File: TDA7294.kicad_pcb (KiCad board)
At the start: 2 copper layers, 81 x 58 mm, 42 parts, among them J1 PAWER, J2 OUT, J3 IN, U1 TDA7294, U2 TDA7294

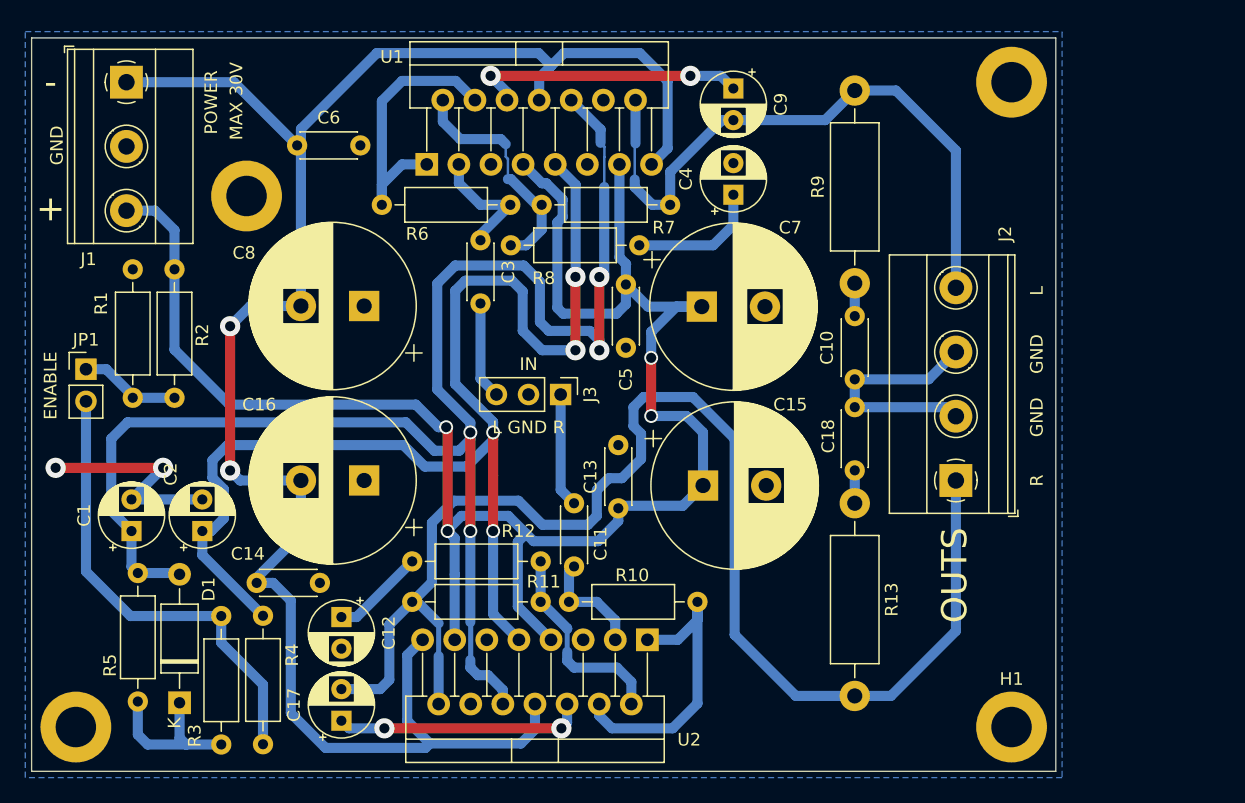
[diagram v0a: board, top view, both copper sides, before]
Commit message: completada version 1.1.0 con TDA al mismo lado
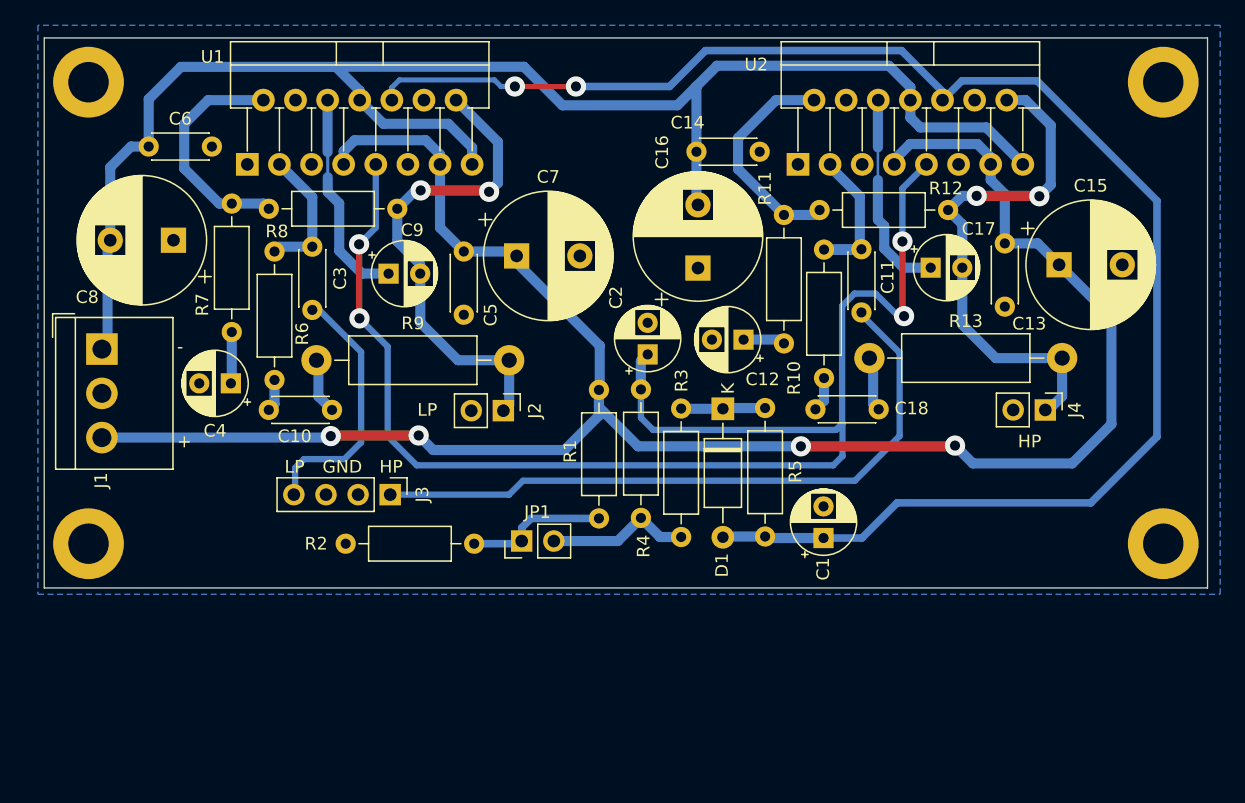
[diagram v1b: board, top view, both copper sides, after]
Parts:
- added J4: Conn_01x02, Connector_PinHeader_2.54mm:PinHeader_1x02_P2.54mm_Vertical, F.Cu at (187.2, 99.4)
- C15, C16, C7, C8: footprint Capacitor_THT:CP_Radial_D13.0mm_P5.00mm -> Capacitor_THT:CP_Radial_D10.0mm_P5.00mm
- J1: footprint TerminalBlock_Phoenix:TerminalBlock_Phoenix_MKDS-1,5-3-5.08_1x03_P5.08mm_Horizontal -> MR-footprint:TerminalBlock_1x03_P3.50mm_Vertical
- J2: value OUT -> Conn_01x02; footprint TerminalBlock_Phoenix:TerminalBlock_Phoenix_MKDS-1,5-4-5.08_1x04_P5.08mm_Horizontal -> Connector_PinHeader_2.54mm:PinHeader_1x02_P2.54mm_Vertical
- J3: footprint Connector_PinHeader_2.54mm:PinHeader_1x03_P2.54mm_Vertical -> Connector_PinHeader_2.54mm:PinHeader_1x04_P2.54mm_Vertical
- moved H2 100.0 mm to (196.5, 73.5)
- moved H3 81.6 mm to (111.5, 110.0)
- moved C17 58.8 mm to (178.1, 88.2), turned to 0 degrees
- moved C1 54.7 mm to (169.6, 109.5)
- moved R12 52.5 mm to (179.5, 83.6), turned to 180 degrees
- moved R5 49.7 mm to (165.0, 109.4), turned to 90 degrees
- moved D1 48.9 mm to (161.7, 99.3), turned to -90 degrees
- moved C14 48.7 mm to (159.6, 79.0)
- moved C10 46.4 mm to (125.8, 99.4), turned to 0 degrees
- moved R3 45.0 mm to (158.4, 99.3), turned to -90 degrees
- moved R9 43.0 mm to (129.5, 95.5), turned to 0 degrees
- moved C4 42.4 mm to (122.8, 97.3), turned to 180 degrees
- moved U2 39.4 mm to (167.6, 80.0), turned to 0 degrees
- moved C12 38.6 mm to (163.3, 93.9), turned to 180 degrees
- moved C2 37.9 mm to (155.7, 95.0)
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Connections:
- J2 pad 1: /OUT2 -> /OUT1
- J3 pad 3: /IN1 -> GND
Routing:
- net GND: track 83.7 -> 5.31 mm, vias 2 -> 0
- net /OUT2: track 111.6 -> 41.3 mm, vias 0 -> 2
- net /IN2: track 9.04 -> 53.2 mm
- net /-VS: track 150.9 -> 124.2 mm, vias 2 -> 0
- net Net-(JP1-B): track 37.1 -> 11.5 mm
- net /+VS: track 146.0 -> 159.4 mm
- net /STBY: track 99.7 -> 112.7 mm
- net /IN1: track 7.72 -> 20.6 mm
- net /OUT1: track 51.0 -> 39.0 mm, vias 0 -> 2
- net Net-(C4-Pad1): track 10.5 -> 4.09 mm
- net Net-(D1-K): track 13.1 -> 6.67 mm
- net Net-(U1-BOOT): track 22.1 -> 16.9 mm, vias 2 -> 0
- net /MUTE: track 121.0 -> 126.1 mm, vias 4 -> 2
- net Net-(U2-+): track 8.77 -> 13.5 mm
- net Net-(C12-Pad1): track 7.42 -> 3.32 mm
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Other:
- board size 81 x 58 mm -> 92 x 43.5 mm
- board text added: "92.0000 mm x 43.5000 mm"
- board text added: "FR4 natural"
- board text added: "Green"
- board text added: "HP"
- board text added: "LP"
- board text removed: "81.0000 mm x 58.0000 mm"
- board text removed: "Black"
- board text removed: "ENABLE"
- board text removed: "IN"
- board text removed: "L"
- board text removed: "L GND R"
- board text removed: "MAX 30V"
- board text removed: "OUTS"
- board text removed: "POWER"
- board text removed: "R"

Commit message: mejorando los conectores
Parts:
- added G***: LOGO, MR-footprint:logo_mr_6x6mm, B.Cu at (152.1, 80.5)
- C10, C13, C14, C18, C5, C6: footprint Capacitor_THT:C_Disc_D4.3mm_W1.9mm_P5.00mm -> Capacitor_THT:C_Disc_D4.7mm_W2.5mm_P5.00mm
- J1: footprint MR-footprint:TerminalBlock_1x03_P3.50mm_Vertical -> Connector_Hirose:Hirose_DF63M-3P-3.96DSA_1x03_P3.96mm_Vertical
- J2, J4: footprint Connector_PinHeader_2.54mm:PinHeader_1x02_P2.54mm_Vertical -> Connector_Molex:Molex_KK-254_AE-6410-02A_1x02_P2.54mm_Vertical
- J3: footprint Connector_PinHeader_2.54mm:PinHeader_1x04_P2.54mm_Vertical -> Connector_Molex:Molex_KK-254_AE-6410-03A_1x03_P2.54mm_Vertical
- moved J1 4.02 mm to (113.0, 94.1)
- moved J4 3.52 mm to (184.3, 101.4), turned to 180 degrees
- moved C14 3.30 mm to (159.6, 75.7)
- moved C16 2.83 mm to (159.3, 85.4)
- moved C6 2.22 mm to (115.9, 76.4)
- moved C8 2.00 mm to (116.9, 84.5)
- moved J2 1.79 mm to (143.6, 101.1), turned to 0 degrees
- moved C15 1.63 mm to (189.8, 87.4)
- moved R2 1.39 mm to (132.6, 111.2)
- moved C7 1.33 mm to (146.1, 86.1)
- moved C2 1.27 mm to (154.8, 94.2)
- moved C12 1.12 mm to (163.0, 92.8)
- moved C13 0.55 mm to (184.5, 86.1)
- moved C18 0.39 mm to (169.2, 99.7)
- moved C10 0.28 mm to (125.7, 99.7)
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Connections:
- J3 pad 3: GND -> /IN1
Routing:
- net /+VS: track 159.4 -> 165.9 mm
- net /OUT2: track 41.3 -> 46.0 mm
- net /-VS: track 124.2 -> 121.0 mm
- net /IN1: track 20.6 -> 17.8 mm
- net /STBY: track 112.7 -> 115.0 mm
- net Net-(U2--): track 17.6 -> 19.8 mm
- net /OUT1: track 39.0 -> 40.9 mm
- net /MUTE: track 126.1 -> 127.2 mm
- net Net-(C12-Pad1): track 3.32 -> 4.06 mm
- net Net-(U1--): track 18.6 -> 19.2 mm
- net GND: track 5.31 -> 5.84 mm
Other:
- board text added: "${COMPANY} ${TITLE} ${REVISION}"
